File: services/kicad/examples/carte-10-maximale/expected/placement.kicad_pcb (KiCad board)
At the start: 2 copper layers, 58.9 x 45.7 mm, 70 parts, among them J1 IN_5V, J10 IO0, J11 IO1, J12 IO2, J13 IO3, J14 IO4, J2 SWD, U1 STM32F103C8T6, U2 AMS1117-3.3

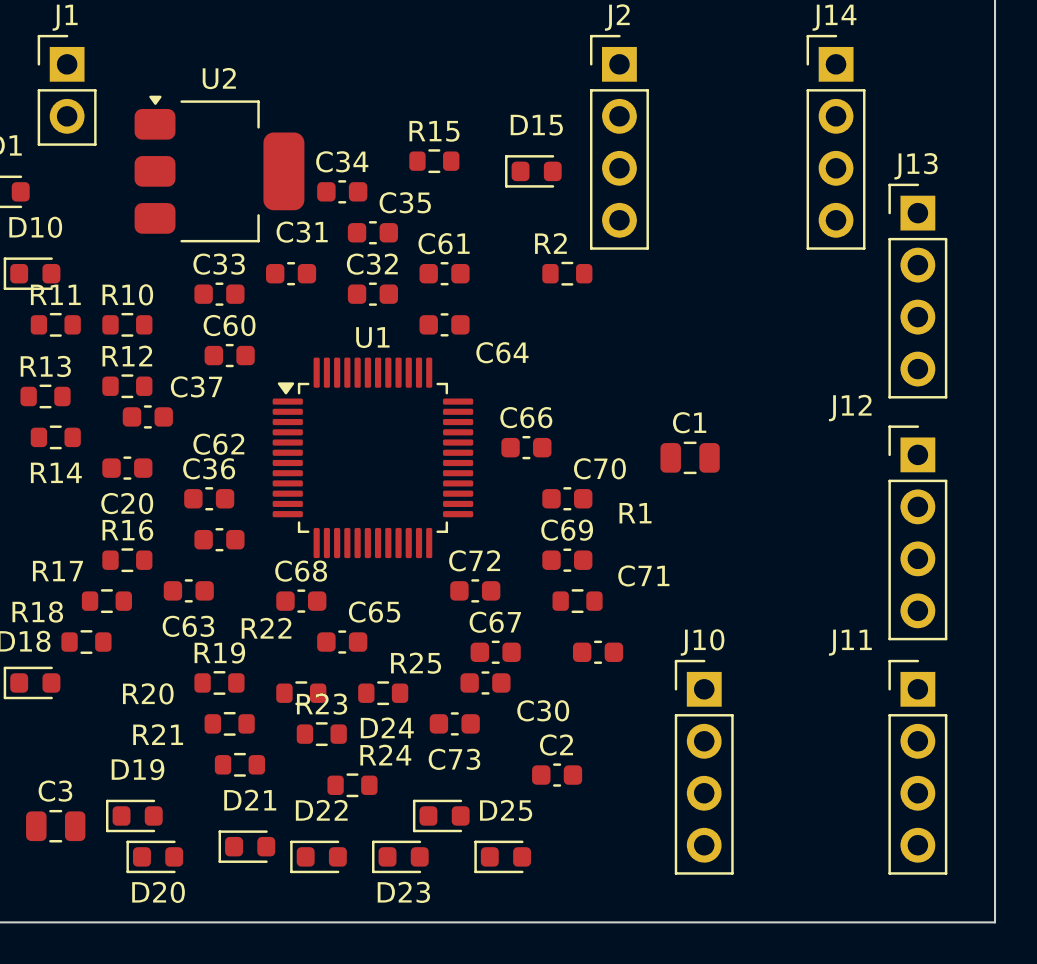
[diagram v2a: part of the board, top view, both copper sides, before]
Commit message: docs(banc): les dix boards du banc du 2026-09-23, service corrige
Artefacts du banc dont le tableau est deja commite : les dix cartes a
100 % route, 0 erreur, 0 connexion manquante, chacune a la taille de son
circuit.

Co-Authored-By: Claude Opus 5 <noreply@anthropic.com>
Claude-Session: https://claude.ai/code/session_01TnMqm4La2CxQHHB5K8aSSV
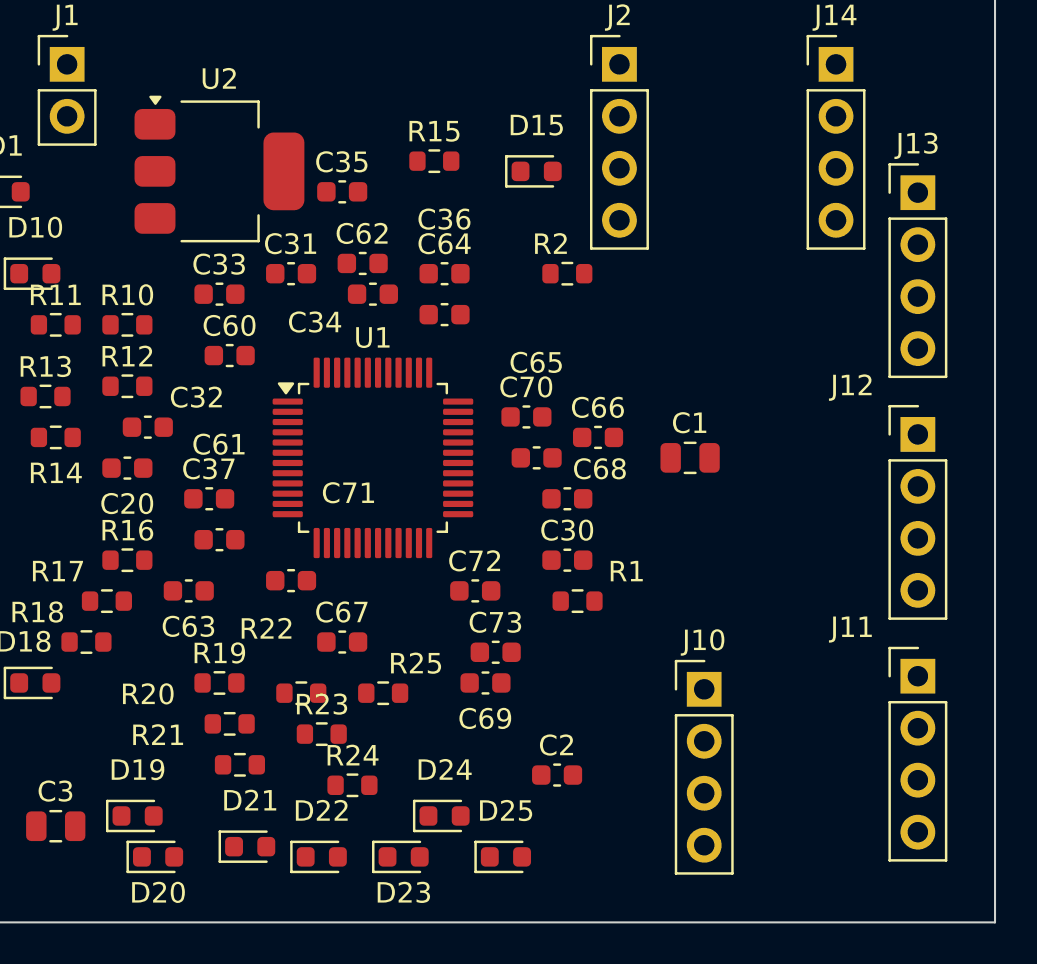
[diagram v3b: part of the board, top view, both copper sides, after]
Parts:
- moved C61 17.0 mm to (101.5, 79.5)
- moved C71 15.4 mm to (105.0, 81.5)
- moved C62 15.2 mm to (108.5, 66.0)
- moved C36 14.6 mm to (112.5, 68.5)
- moved C68 13.9 mm to (118.5, 77.5)
- moved C65 13.1 mm to (117.0, 75.5)
- moved C32 12.8 mm to (98.0, 74.0)
- moved C67 7.52 mm to (107.5, 84.5)
- moved C30 7.21 mm to (118.5, 80.5)
- moved C69 7.21 mm to (114.5, 86.5)
- moved C34 5.22 mm to (109.0, 67.5)
- moved C37 5.00 mm to (101.0, 77.5)
- moved C70 4.47 mm to (116.5, 73.5)
- moved C73 4.03 mm to (115.0, 85.0)
- moved C66 3.54 mm to (120.0, 74.5)
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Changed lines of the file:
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@@
 		(tags "resistor")
 		(property "Reference" "R1"
-			(at 2.82843 -4.25843 0)
+			(at 2.4 -1.43 0)
 			(layer "F.SilkS")
 			(effects
@@
 		(generator "kicad-footprint-generator")
 		(layer "F.Cu")
-		(at 114.5 86.5)
+		(at 118.5 80.5)
 		(descr "Capacitor SMD 0603 (1608 Metric), square (rectangular) end terminal, IPC-7351 nominal, (Body size source: IPC-SM-782 page 76, https://www.pcb-3d.com/wordpress/wp-content/uploads/ipc-sm-782a_amendment_1_and_2.pdf)")
 		(tags "capacitor")
 		(property "Reference" "C30"
-			(at 2.82843 1.39843 0)
+			(at 0 -1.43 0)
 			(layer "F.SilkS")
 			(effects
@@
 		(tags "capacitor")
 		(property "Reference" "C31"
-			(at 0.565685 -1.99569 0)
+			(at 0 -1.43 0)
 			(layer "F.SilkS")
 			(effects
@@
 		(generator "kicad-footprint-generator")
 		(layer "F.Cu")
-		(at 109 67.5)
+		(at 98 74)
 		(descr "Capacitor SMD 0603 (1608 Metric), square (rectangular) end terminal, IPC-7351 nominal, (Body size source: IPC-SM-782 page 76, https://www.pcb-3d.com/wordpress/wp-content/uploads/ipc-sm-782a_amendment_1_and_2.pdf)")
 		(tags "capacitor")
 		(property "Reference" "C32"
-			(at 0 -1.43 0)
+			(at 2.4 -1.43 0)
 			(layer "F.SilkS")
 			(effects
@@
 		(generator "kicad-footprint-generator")
 		(layer "F.Cu")
-		(at 107.5 62.5)
+		(at 109 67.5)
 		(descr "Capacitor SMD 0603 (1608 Metric), square (rectangular) end terminal, IPC-7351 nominal, (Body size source: IPC-SM-782 page 76, https://www.pcb-3d.com/wordpress/wp-content/uploads/ipc-sm-782a_amendment_1_and_2.pdf)")
 		(tags "capacitor")
 		(property "Reference" "C34"
-			(at 0 -1.43 0)
+			(at -2.82843 1.39843 0)
 			(layer "F.SilkS")
 			(effects
@@
 		(generator "kicad-footprint-generator")
 		(layer "F.Cu")
-		(at 109 64.5)
+		(at 107.5 62.5)
 		(descr "Capacitor SMD 0603 (1608 Metric), square (rectangular) end terminal, IPC-7351 nominal, (Body size source: IPC-SM-782 page 76, https://www.pcb-3d.com/wordpress/wp-content/uploads/ipc-sm-782a_amendment_1_and_2.pdf)")
 		(tags "capacitor")
 		(property "Reference" "C35"
-			(at 1.6 -1.43 0)
+			(at 0 -1.43 0)
 			(layer "F.SilkS")
 			(effects
@@
 		(generator "kicad-footprint-generator")
 		(layer "F.Cu")
-		(at 101 77.5)
+		(at 112.5 68.5)
 		(descr "Capacitor SMD 0603 (1608 Metric), square (rectangular) end terminal, IPC-7351 nominal, (Body size source: IPC-SM-782 page 76, https://www.pcb-3d.com/wordpress/wp-content/uploads/ipc-sm-782a_amendment_1_and_2.pdf)")
 		(tags "capacitor")
 		(property "Reference" "C36"
-			(at 0 -1.43 0)
+			(at -5.8783e-16 -4.63 0)
 			(layer "F.SilkS")
 			(effects
@@
 		(generator "kicad-footprint-generator")
 		(layer "F.Cu")
-		(at 98 73.5)
+		(at 101 77.5)
 		(descr "Capacitor SMD 0603 (1608 Metric), square (rectangular) end terminal, IPC-7351 nominal, (Body size source: IPC-SM-782 page 76, https://www.pcb-3d.com/wordpress/wp-content/uploads/ipc-sm-782a_amendment_1_and_2.pdf)")
 		(tags "capacitor")
 		(property "Reference" "C37"
-			(at 2.4 -1.43 0)
+			(at 0 -1.43 0)
 			(layer "F.SilkS")
 			(effects
@@
 		(tags "resistor")
 		(property "Reference" "R24"
-			(at 1.6 -1.43 0)
+			(at 0 -1.43 0)
 			(layer "F.SilkS")
 			(effects
@@
 		(tags "LED")
 		(property "Reference" "D24"
-			(at -2.82843 -4.25843 0)
+			(at -1.46958e-16 -2.23 0)
 			(layer "F.SilkS")
 			(effects
@@
 		(generator "kicad-footprint-generator")
 		(layer "F.Cu")
-		(at 135.63 86.81)
+		(at 135.63 86.1706)
 		(descr "Through hole straight pin header, 1x04, 2.54mm pitch, single row")
 		(tags "Through hole pin header THT 1x04 2.54mm single row")
@@
 		(generator "kicad-footprint-generator")
 		(layer "F.Cu")
-		(at 135.63 75.3553)
+		(at 135.63 74.3553)
 		(descr "Through hole straight pin header, 1x04, 2.54mm pitch, single row")
 		(tags "Through hole pin header THT 1x04 2.54mm single row")
@@
 		(generator "kicad-footprint-generator")
 		(layer "F.Cu")
-		(at 135.63 63.54)
+		(at 135.63 62.54)
 		(descr "Through hole straight pin header, 1x04, 2.54mm pitch, single row")
 		(tags "Through hole pin header THT 1x04 2.54mm single row")
@@
 		(generator "kicad-footprint-generator")
 		(layer "F.Cu")
-		(at 112.5 66.5)
+		(at 101.5 79.5)
 		(descr "Capacitor SMD 0603 (1608 Metric), square (rectangular) end terminal, IPC-7351 nominal, (Body size source: IPC-SM-782 page 76, https://www.pcb-3d.com/wordpress/wp-content/uploads/ipc-sm-782a_amendment_1_and_2.pdf)")
 		(tags "capacitor")
 		(property "Reference" "C61"
-			(at 0 -1.43 0)
+			(at -5.8783e-16 -4.63 0)
 			(layer "F.SilkS")
 			(effects
@@
 		(generator "kicad-footprint-generator")
 		(layer "F.Cu")
-		(at 101.5 79.5)
+		(at 108.5 66)
 		(descr "Capacitor SMD 0603 (1608 Metric), square (rectangular) end terminal, IPC-7351 nominal, (Body size source: IPC-SM-782 page 76, https://www.pcb-3d.com/wordpress/wp-content/uploads/ipc-sm-782a_amendment_1_and_2.pdf)")
 		(tags "capacitor")
 		(property "Reference" "C62"
-			(at -5.8783e-16 -4.63 0)
+			(at 0 -1.43 0)
 			(layer "F.SilkS")
 			(effects
@@
 		(generator "kicad-footprint-generator")
 		(layer "F.Cu")
-		(at 112.5 69)
+		(at 112.5 66.5)
 		(descr "Capacitor SMD 0603 (1608 Metric), square (rectangular) end terminal, IPC-7351 nominal, (Body size source: IPC-SM-782 page 76, https://www.pcb-3d.com/wordpress/wp-content/uploads/ipc-sm-782a_amendment_1_and_2.pdf)")
 		(tags "capacitor")
 		(property "Reference" "C64"
-			(at 2.82843 1.39843 0)
+			(at 0 -1.43 0)
 			(layer "F.SilkS")
 			(effects
@@
 		(generator "kicad-footprint-generator")
 		(layer "F.Cu")
-		(at 107.5 84.5)
+		(at 117 75.5)
 		(descr "Capacitor SMD 0603 (1608 Metric), square (rectangular) end terminal, IPC-7351 nominal, (Body size source: IPC-SM-782 page 76, https://www.pcb-3d.com/wordpress/wp-content/uploads/ipc-sm-782a_amendment_1_and_2.pdf)")
 		(tags "capacitor")
 		(property "Reference" "C65"
-			(at 1.6 -1.43 0)
+			(at -5.8783e-16 -4.63 0)
 			(layer "F.SilkS")
 			(effects
@@
 		(generator "kicad-footprint-generator")
 		(layer "F.Cu")
-		(at 116.5 75)
+		(at 120 74.5)
 		(descr "Capacitor SMD 0603 (1608 Metric), square (rectangular) end terminal, IPC-7351 nominal, (Body size source: IPC-SM-782 page 76, https://www.pcb-3d.com/wordpress/wp-content/uploads/ipc-sm-782a_amendment_1_and_2.pdf)")
 		(tags "capacitor")
@@
 		(generator "kicad-footprint-generator")
 		(layer "F.Cu")
-		(at 115 85)
+		(at 107.5 84.5)
 		(descr "Capacitor SMD 0603 (1608 Metric), square (rectangular) end terminal, IPC-7351 nominal, (Body size source: IPC-SM-782 page 76, https://www.pcb-3d.com/wordpress/wp-content/uploads/ipc-sm-782a_amendment_1_and_2.pdf)")
 		(tags "capacitor")
@@
 		(generator "kicad-footprint-generator")
 		(layer "F.Cu")
-		(at 105.5 82.5)
+		(at 118.5 77.5)
 		(descr "Capacitor SMD 0603 (1608 Metric), square (rectangular) end terminal, IPC-7351 nominal, (Body size source: IPC-SM-782 page 76, https://www.pcb-3d.com/wordpress/wp-content/uploads/ipc-sm-782a_amendment_1_and_2.pdf)")
 		(tags "capacitor")
 		(property "Reference" "C68"
-			(at 0 -1.43 0)
+			(at 1.6 -1.43 0)
 			(layer "F.SilkS")
 			(effects
@@
 		(generator "kicad-footprint-generator")
 		(layer "F.Cu")
-		(at 118.5 80.5)
+		(at 114.5 86.5)
 		(descr "Capacitor SMD 0603 (1608 Metric), square (rectangular) end terminal, IPC-7351 nominal, (Body size source: IPC-SM-782 page 76, https://www.pcb-3d.com/wordpress/wp-content/uploads/ipc-sm-782a_amendment_1_and_2.pdf)")
 		(tags "capacitor")
 		(property "Reference" "C69"
-			(at 0 -1.43 0)
+			(at 1.95943e-16 1.77 0)
 			(layer "F.SilkS")
 			(effects
@@
 		(generator "kicad-footprint-generator")
 		(layer "F.Cu")
-		(at 118.5 77.5)
+		(at 116.5 73.5)
 		(descr "Capacitor SMD 0603 (1608 Metric), square (rectangular) end terminal, IPC-7351 nominal, (Body size source: IPC-SM-782 page 76, https://www.pcb-3d.com/wordpress/wp-content/uploads/ipc-sm-782a_amendment_1_and_2.pdf)")
 		(tags "capacitor")
 		(property "Reference" "C70"
-			(at 1.6 -1.43 0)
+			(at 0 -1.43 0)
 			(layer "F.SilkS")
 			(effects
@@
 		(generator "kicad-footprint-generator")
 		(layer "F.Cu")
-		(at 120 85)
+		(at 105 81.5)
 		(descr "Capacitor SMD 0603 (1608 Metric), square (rectangular) end terminal, IPC-7351 nominal, (Body size source: IPC-SM-782 page 76, https://www.pcb-3d.com/wordpress/wp-content/uploads/ipc-sm-782a_amendment_1_and_2.pdf)")
 		(tags "capacitor")
 		(property "Reference" "C71"
-			(at 2.26274 -3.69274 0)
+			(at 2.82843 -4.25843 0)
 			(layer "F.SilkS")
 			(effects
@@
 		(generator "kicad-footprint-generator")
 		(layer "F.Cu")
-		(at 113 88.5)
+		(at 115 85)
 		(descr "Capacitor SMD 0603 (1608 Metric), square (rectangular) end terminal, IPC-7351 nominal, (Body size source: IPC-SM-782 page 76, https://www.pcb-3d.com/wordpress/wp-content/uploads/ipc-sm-782a_amendment_1_and_2.pdf)")
 		(tags "capacitor")
 		(property "Reference" "C73"
-			(at 1.95943e-16 1.77 0)
+			(at 0 -1.43 0)
 			(layer "F.SilkS")
 			(effects

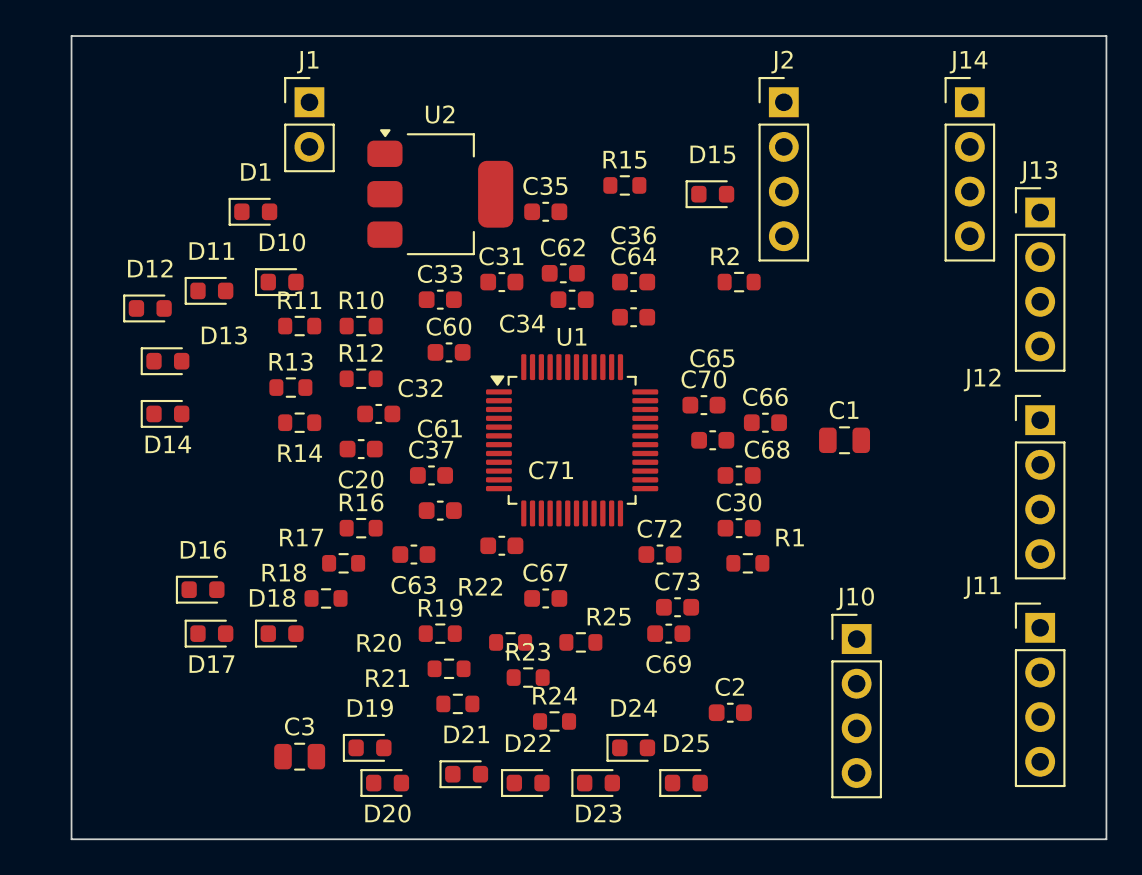
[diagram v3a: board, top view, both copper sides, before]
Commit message: fix(banc): le banc route comme la production — plafond 8, budget du client
D-2026-09-24-f. run_pipeline.py prenait 2 couches et 1800 s par défaut, et
carte-07 écrivait 2 en dur : dix cartes sur quinze ne pouvaient jamais
escalader, et la règle « toute connexion manquante fait monter » était
inerte dans le banc. Mesuré sur carte-07 : 97 %, seule la masse manquante,
« le palier suivant sera tenté »… puis retour à 2 couches.

Plafond par défaut 8 (client Pro Max), budget min(600 + 300 x plafond, 3600)
comme routingSearchBudgetS côté client. En production, rien ne change : le
plafond reste celui du plan.

Livraisons du jour, toutes vérifiées par kicad-cli et contre le schéma
(0 erreur bloquante, 0 connexion manquante, 0 court-circuit) :
carte-04, 05, 06, 08 (campagne de l'après-midi) et carte-09, 10 (4 couches).
Les boards versionnés de ces cartes court-circuitaient des nets du schéma.

Correction de ma propre erreur dans la doc : carte-07 n'avait jamais
escaladé ; les lignes « palier 4 et 6 » du journal étaient celles de
carte-08, démarrée la même minute.

Co-Authored-By: Claude Opus 5.5 <noreply@anthropic.com>
Claude-Session: https://claude.ai/code/session_01TnMqm4La2CxQHHB5K8aSSV
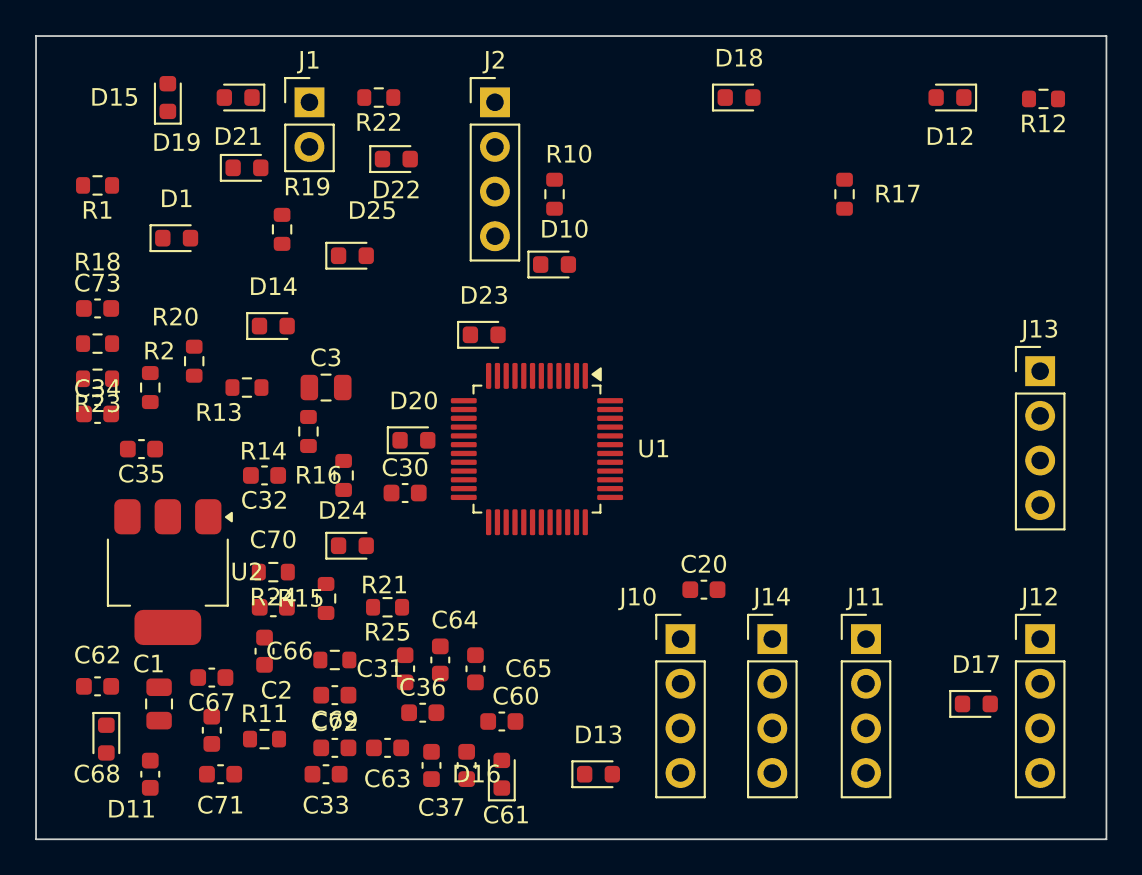
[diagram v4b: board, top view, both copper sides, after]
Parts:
- moved D12 47.1 mm to (130.5, 56.0), turned to 180 degrees
- moved D17 43.7 mm to (132.0, 90.5)
- moved R1 42.8 mm to (82.0, 61.0), turned to 180 degrees
- moved R12 42.0 mm to (135.8, 56.1), turned to 180 degrees
- moved C1 41.8 mm to (85.5, 90.5), turned to 270 degrees
- moved D21 40.6 mm to (90.0, 56.0), turned to 180 degrees
- moved D18 40.1 mm to (118.5, 56.0)
- moved C68 37.6 mm to (85.0, 94.5), turned to 90 degrees
- moved C73 37.1 mm to (82.0, 68.0)
- moved D22 36.3 mm to (99.0, 59.5)
- moved D25 35.5 mm to (96.5, 65.0)
- moved C62 35.4 mm to (82.0, 89.5), turned to 180 degrees
- moved R17 35.4 mm to (124.5, 61.5), turned to 270 degrees
- moved D13 33.9 mm to (110.5, 94.5)
- moved D19 33.7 mm to (90.5, 60.0)
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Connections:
- C3 pad 1: Net-(C3-1) -> +3V3
- U1 pad 36: PWR_FLAG -> +3V3
- U1 pad 48: PWR_FLAG -> +3V3
- U1 pad 9: PWR_FLAG -> IO_L5
- U2 pad 2: Net-(U2-2) -> +3V3
- U2 pad 3: PWR_FLAG -> VIN
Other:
- board size 58.9 x 45.7 mm -> 60.9 x 45.7 mm
